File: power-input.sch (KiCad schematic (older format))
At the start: 18 parts, among them J301 Conn_01x02, Q301 WST03P06, U301 SY8401

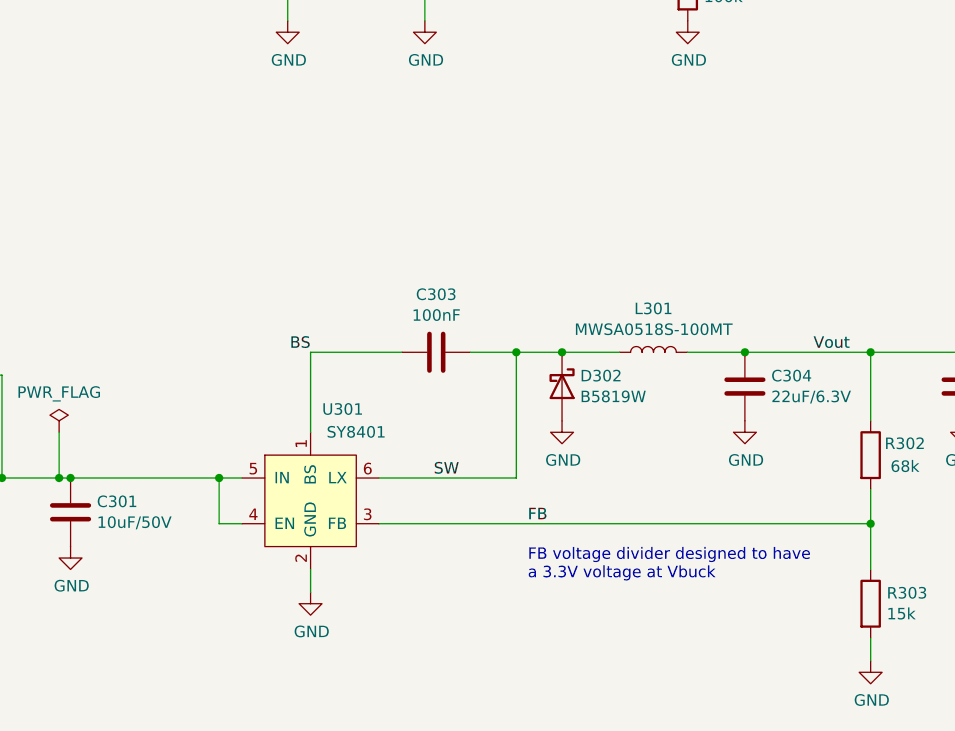
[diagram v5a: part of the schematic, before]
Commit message: Change optocoupler types, improve ground planes and a lot of other smaller fixes
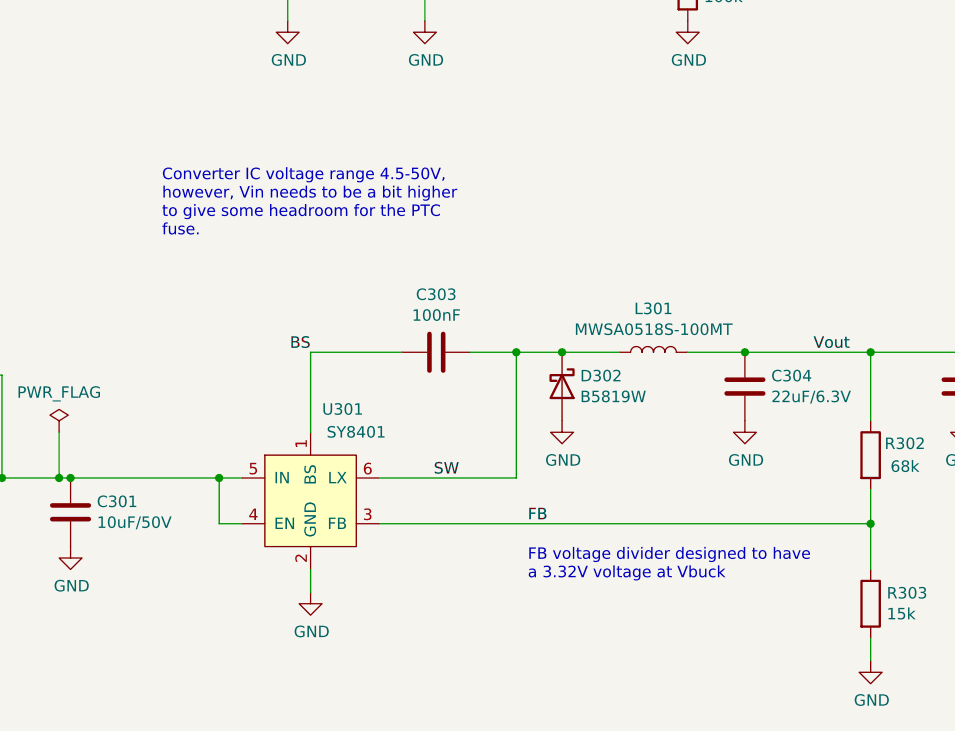
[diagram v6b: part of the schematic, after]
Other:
- note added: "Converter IC voltage range 4.5-50V,\nhowever, Vin needs to be a bit higher\nto give some headroom for the PTC\nfuse."
- note added: "FB voltage divider designed to have\na 3.32V voltage at Vbuck"
- note removed: "FB voltage divider designed to have\na 3.3V voltage at Vbuck"
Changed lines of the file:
@@
 $EndComp
 Text Notes 5850 5250 0    50   ~ 0
-FB voltage divider designed to have\na 3.3V voltage at Vbuck
+FB voltage divider designed to have\na 3.32V voltage at Vbuck
 Wire Wire Line
 	4900 4250 4900 4600
@@
 Text GLabel 2600 4350 0    50   Input ~ 0
 USB_5V
+Text Notes 4250 3750 0    50   ~ 0
+Converter IC voltage range 4.5-50V,\nhowever, Vin needs to be a bit higher\nto give some headroom for the PTC\nfuse.
 $EndSCHEMATC

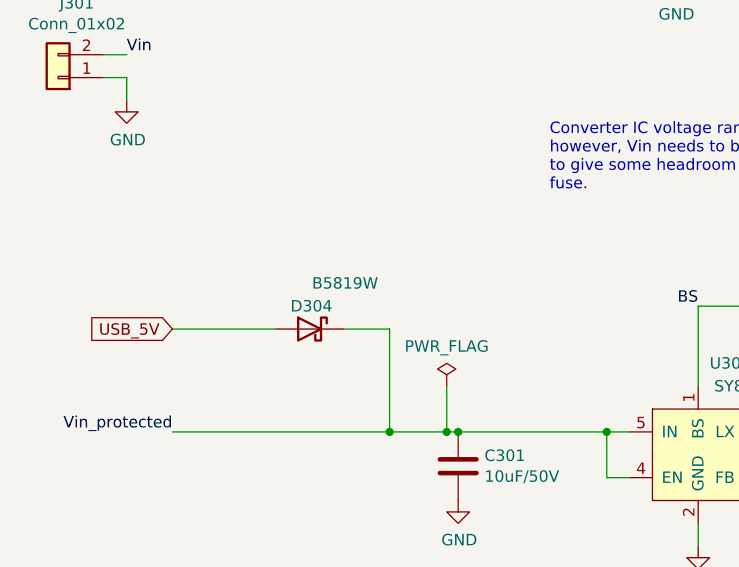
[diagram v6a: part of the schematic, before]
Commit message: Swap optocoupler GPIO pins to connect DAC to output
Not that it makes a lot of difference: the inverting
NPN will behave as a hard switch nevertheless
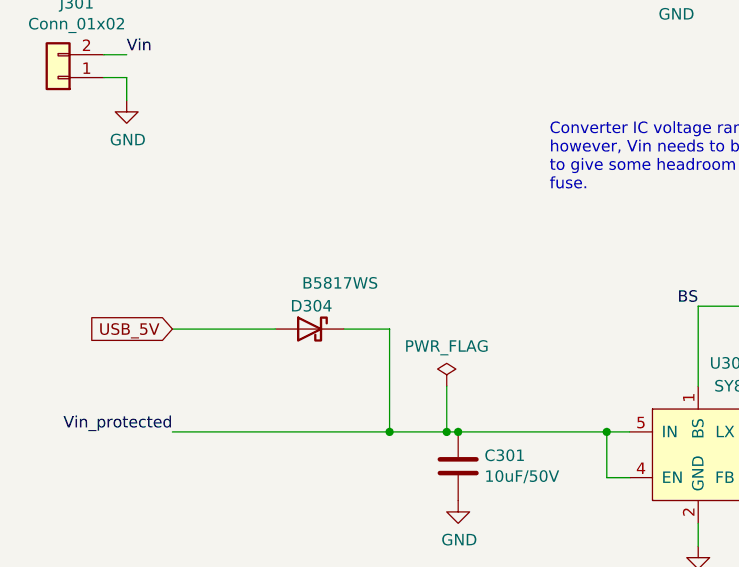
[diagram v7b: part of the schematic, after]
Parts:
- D304: value B5819W -> B5817WS; footprint Diode_SMD:D_SOD-123 -> Diode_SMD:D_SOD-323; LCSC C8598 -> C123899
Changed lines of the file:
@@
 AR Path="/5F6FAF6E/5FAEC660" Ref="D304"  Part="1"
 F 0 "D304" H 3100 4450 50  0000 L CNN
-F 1 "B5819W" H 2900 4550 50  0000 L CNN
-F 2 "Diode_SMD:D_SOD-123" H 3200 4350 50  0001 C CNN
+F 1 "B5817WS" H 2900 4550 50  0000 L CNN
+F 2 "Diode_SMD:D_SOD-323" H 3200 4350 50  0001 C CNN
 F 3 "~" H 3200 4350 50  0001 C CNN
 F 4 "" V 3200 4350 50  0001 C CNN "Notes"
-F 5 "C8598" H 3200 4350 50  0001 C CNN "LCSC"
+F 5 "C123899" H 3200 4350 50  0001 C CNN "LCSC"
 	1    3200 4350
 	-1   0    0    -1

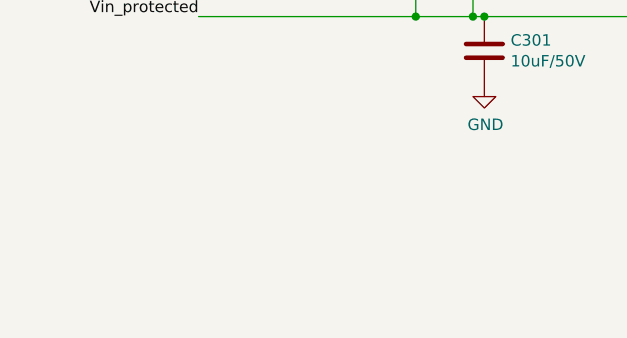
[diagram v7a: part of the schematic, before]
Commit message: Revamp Prototype Area for external I/O connector and accomodate 'Hat' / Daughter board.
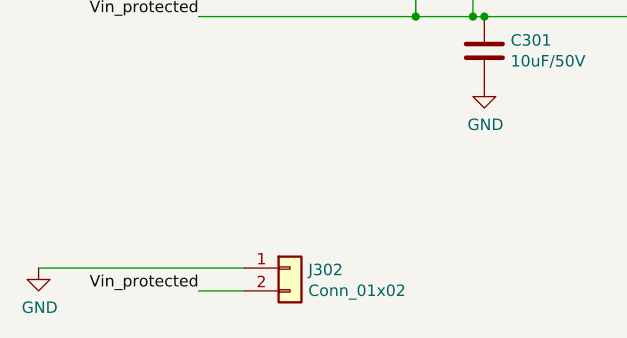
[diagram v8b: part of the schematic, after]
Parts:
- added J302: Conn_01x02, Connector_PinHeader_2.54mm:PinHeader_1x02_P2.54mm_Vertical, symbol Connector_Generic:Conn_01x02
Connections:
- net GND: now also J302.1 (Pin_1)
- net Vin_protected: now also J302.2 (Pin_2)
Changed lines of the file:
@@
 Text Notes 4250 3750 0    50   ~ 0
 Converter IC voltage range 4.5-50V,\nhowever, Vin needs to be a bit higher\nto give some headroom for the PTC\nfuse.
+$Comp
+L Connector_Generic:Conn_01x02 J?
+U 1 1 5FB1656B
+P 3000 5900
+AR Path="/5FC3847D/5FB1656B" Ref="J?"  Part="1"
+AR Path="/5F6FAF6E/5FB1656B" Ref="J302"  Part="1"
+F 0 "J302" H 3080 5892 50  0000 L CNN
+F 1 "Conn_01x02" H 3080 5801 50  0000 L CNN
+F 2 "Connector_PinHeader_2.54mm:PinHeader_1x02_P2.54mm_Vertical" H 3000 5900 50  0001 C CNN
+F 3 "~" H 3000 5900 50  0001 C CNN
+F 4 "C376075" H 3000 5900 50  0001 C CNN "LCSC"
+	1    3000 5900
+	1    0    0    -1
+$EndComp
+$Comp
+L power:GND #PWR?
+U 1 1 5FB16571
+P 1900 5900
+AR Path="/5FC3847D/5FB16571" Ref="#PWR?"  Part="1"
+AR Path="/5F6FAF6E/5FB16571" Ref="#PWR0107"  Part="1"
+F 0 "#PWR0107" H 1900 5650 50  0001 C CNN
+F 1 "GND" H 1905 5727 50  0000 C CNN
+F 2 "" H 1900 5900 50  0001 C CNN
+F 3 "" H 1900 5900 50  0001 C CNN
+	1    1900 5900
+	1    0    0    -1
+$EndComp
+Wire Wire Line
+	1900 5900 2800 5900
+Text Label 2600 6000 2    50   ~ 0
+Vin_protected
+Wire Wire Line
+	2800 6000 2600 6000
 $EndSCHEMATC
